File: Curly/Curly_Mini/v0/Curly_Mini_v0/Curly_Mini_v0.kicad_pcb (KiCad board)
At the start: 2 copper layers, 17 parts, among them U1 RP2040, U2 MCP25625T-E_ML, U4 W25Q16JVUXIQ_TR, Y2 12.000 MHz, C9002

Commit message: Curly Mini almost done :)
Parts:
- added C10: 100n, Capacitor_SMD:C_0402_1005Metric, F.Cu at (92.8, 58.1)
- added C11: 2u2, Capacitor_SMD:C_0402_1005Metric, F.Cu at (93.8, 57.1)
- added C12: 100n, Capacitor_SMD:C_0402_1005Metric, F.Cu at (78.1, 76.3)
- added C13: 2u2, Capacitor_SMD:C_0402_1005Metric, F.Cu at (79.8, 59.3)
- added C14: 100n, Capacitor_SMD:C_0402_1005Metric, F.Cu at (80.7, 59.3)
- added C15: 2u2, Capacitor_SMD:C_0402_1005Metric, F.Cu at (84.5, 52.2)
- added C16: 100n, Capacitor_SMD:C_0402_1005Metric, F.Cu at (84.5, 53.2)
- added C17: 100n, Capacitor_SMD:C_0402_1005Metric, F.Cu at (85.1, 64.5)
- added C18: 100n, Capacitor_SMD:C_0402_1005Metric, F.Cu at (89.3, 65.5)
- added C19: 2u2, Capacitor_SMD:C_0402_1005Metric, F.Cu at (84.2, 64.5)
- added C9: 2u2, Capacitor_SMD:C_0402_1005Metric, F.Cu at (82.2, 59.5)
- added J1: DEBUG_PORT, Connector_JST:JST_SH_BM03B-SRSS-TB_1x03-1MP_P1.00mm_Vertical, F.Cu at (75.8, 58.8)
- added J2: Conn_01x01_Pin, ICDB_Waffle:ICDB_Castellated_Pad, F.Cu at (121.0, 60.1)
- added J3: Conn_01x01_Pin, ICDB_Waffle:ICDB_Castellated_Pad, F.Cu at (121.0, 57.5)
- FB1: footprint Capacitor_SMD:C_0402_1005Metric -> Inductor_SMD:L_0603_1608Metric
- moved U4 25.9 mm to (80.7, 63.1), turned to 90 degrees
- moved FB1 25.4 mm to (84.2, 54.5), turned to 180 degrees
- moved C3 23.2 mm to (81.8, 55.8), turned to 180 degrees
- moved R4 22.2 mm to (80.2, 56.2), turned to -90 degrees
- moved C6 21.9 mm to (94.8, 56.7), turned to 90 degrees
- moved R3 21.7 mm to (79.2, 56.2), turned to -90 degrees
- moved C4 21.6 mm to (81.8, 54.5), turned to 180 degrees
- moved C5 21.2 mm to (83.3, 56.2), turned to 90 degrees
- moved C2 20.3 mm to (81.8, 56.8), turned to 180 degrees
- moved R1 19.4 mm to (81.6, 76.8)
- moved C7 18.7 mm to (97.6, 56.1), turned to 45 degrees
- moved Y2 17.0 mm to (98.5, 58.6), turned to 45 degrees
- moved C8 16.4 mm to (99.3, 61.0), turned to 45 degrees
- moved C1 15.8 mm to (79.5, 60.7), turned to 180 degrees
- moved U1 9.61 mm to (88.0, 59.4), turned to 90 degrees
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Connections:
- U1 pad 13: /SPI1_SCK -> unconnected-(U1-GPIO10-Pad13)
- U1 pad 14: /SPI1_TX -> unconnected-(U1-GPIO11-Pad14)
- U1 pad 17: unconnected-(U1-GPIO14-Pad17) -> /SPI1_SCK
- U1 pad 18: unconnected-(U1-GPIO15-Pad18) -> /SPI1_TX
- U2 pad 12: unconnected-(U2-CANL-Pad12) -> /CANL
- U2 pad 13: unconnected-(U2-CANH-Pad13) -> /CANH
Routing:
- net +1V1: track 0.00 -> 28.8 mm
- net +3V3: track 0.00 -> 22.5 mm, vias 0 -> 7
- net /SWCLK: track 0.00 -> 16.0 mm, vias 0 -> 2
- net /SWDIO: track 0.00 -> 15.3 mm, vias 0 -> 2
- net /SPI1_CSn: track 0.00 -> 14.9 mm
- net /SPI1_RX: track 0.00 -> 14.6 mm, vias 0 -> 2
- net /SPI1_TX: track 0.00 -> 14.5 mm, vias 0 -> 2
- net /SPI1_SCK: track 0.00 -> 14.4 mm
- net GND: track 0.00 -> 9.15 mm, vias 0 -> 41
- net /XIN: track 0.00 -> 8.95 mm
- net /~{QSPI_CSN}: track 0.00 -> 8.72 mm
- net /QSPI_SD1: track 0.00 -> 8.01 mm
- net /QSPI_SD2: track 0.00 -> 7.31 mm
- net Net-(U1-USB_DP): track 0.00 -> 6.11 mm
- net Net-(U1-USB_DM): track 0.00 -> 5.34 mm
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- added copper zone on F.Cu, net +3V3
- added copper zone on In1.Cu, net +3V3
- added copper zone on F.Cu, net GND
- added copper zone on In2.Cu, net GND
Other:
- copper layers 2 -> 4

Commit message: Curly Mini almost done (again) :)
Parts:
- removed C12: 100n, Capacitor_SMD:C_0402_1005Metric
- added C20: 10u, Capacitor_SMD:C_0603_1608Metric, F.Cu at (145.9, 56.9)
- added C21: 100n, Capacitor_SMD:C_0402_1005Metric, F.Cu at (142.4, 47.7)
- added C22: 10u, Capacitor_SMD:C_0603_1608Metric, F.Cu at (145.9, 59.4)
- added C23: 100n, Capacitor_SMD:C_0402_1005Metric, F.Cu at (142.4, 49.7)
- added C24: 100n, Capacitor_SMD:C_0402_1005Metric, F.Cu at (142.4, 51.6)
- added C25: 100n, Capacitor_SMD:C_0402_1005Metric, F.Cu at (105.7, 55.3)
- added C26: 100n, Capacitor_SMD:C_0402_1005Metric, F.Cu at (106.2, 63.8)
- added C27: 100n, Capacitor_SMD:C_0402_1005Metric, F.Cu at (142.4, 57.5)
- added C28: 2u2, Capacitor_SMD:C_0402_1005Metric, F.Cu at (142.4, 59.5)
- added C29: 2u2, Capacitor_SMD:C_0402_1005Metric, F.Cu at (105.7, 54.3)
- added U3: XC6206PxxxMR, Package_TO_SOT_SMD:SOT-23-3, F.Cu at (146.4, 48.9)
- added U5: SE8650X2-HF, Package_TO_SOT_SMD:SOT-23-3, F.Cu at (146.4, 53.4)
- moved R1 25.0 mm to (92.8, 54.5), turned to 180 degrees
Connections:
- U1 pad 11: unconnected-(U1-GPIO8-Pad11) -> /~{CAN_TX2_RTS}
- U1 pad 12: unconnected-(U1-GPIO9-Pad12) -> /~{CAN_TX1_RTS}
- U1 pad 13: unconnected-(U1-GPIO10-Pad13) -> /~{CAN_TX0_RTS}
- U1 pad 14: unconnected-(U1-GPIO11-Pad14) -> /~{CAN_RESET}
- U1 pad 27: unconnected-(U1-GPIO16-Pad27) -> /~{CAN_RX_INT}
- U1 pad 28: unconnected-(U1-GPIO17-Pad28) -> /~{CAN_RX_BUF0}
- U1 pad 29: unconnected-(U1-GPIO18-Pad29) -> /~{CAN_RX_BUF1}
- U1 pad 30: unconnected-(U1-GPIO19-Pad30) -> /MCP25625_CLK
- U1 pad 31: unconnected-(U1-GPIO20-Pad31) -> /CAN_TXVR_STBY
- U2 pad 10: unconnected-(U2-RXD-Pad10) -> Net-(U2-RXCAN)
- U2 pad 11: unconnected-(U2-VIO-Pad11) -> +3V3
- U2 pad 16: unconnected-(U2-TXD-Pad16) -> Net-(U2-TXCAN)
- U2 pad 18: unconnected-(U2-VSS-Pad18) -> GND
- U2 pad 19: unconnected-(U2-VDDA-Pad19) -> +5V
- U2 pad 2: unconnected-(U2-~{RESET}-Pad2) -> /~{CAN_RESET}
- U2 pad 21: unconnected-(U2-OSC1-Pad21) -> /MCP25625_CLK
- U2 pad 22: unconnected-(U2-GND-Pad22) -> GND
- U2 pad 23: unconnected-(U2-~{RX1BF}-Pad23) -> /~{CAN_RX_BUF1}
- U2 pad 24: unconnected-(U2-~{RX0BF}-Pad24) -> /~{CAN_RX_BUF0}
- U2 pad 25: unconnected-(U2-~{INT}-Pad25) -> /~{CAN_RX_INT}
- U2 pad 29: unconnected-(U2-EP-Pad29) -> GND
- U2 pad 3: unconnected-(U2-VDD-Pad3) -> +3V3
- U2 pad 4: unconnected-(U2-TXCAN-Pad4) -> Net-(U2-TXCAN)
- U2 pad 5: unconnected-(U2-RXCAN-Pad5) -> Net-(U2-RXCAN)
- U2 pad 7: unconnected-(U2-~{TX0RTS}-Pad7) -> /~{CAN_TX0_RTS}
- U2 pad 8: unconnected-(U2-~{TX1RTS}-Pad8) -> /~{CAN_TX1_RTS}
- U2 pad 9: unconnected-(U2-~{TX2RTS}-Pad9) -> /~{CAN_TX2_RTS}
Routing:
- net /~{CAN_TX2_RTS}: track 0.00 -> 26.6 mm
- net /CAN_TXVR_STBY: track 0.00 -> 23.9 mm
- net /~{CAN_TX1_RTS}: track 0.00 -> 23.7 mm
- net /~{CAN_TX0_RTS}: track 0.00 -> 21.6 mm
- net /MCP25625_CLK: track 0.00 -> 18.1 mm
- net /~{CAN_RESET}: track 0.00 -> 16.7 mm
- net /~{CAN_RX_BUF1}: track 0.00 -> 16.6 mm
- net /~{CAN_RX_INT}: track 0.00 -> 15.9 mm
- net /~{CAN_RX_BUF0}: track 0.00 -> 15.5 mm
- net Net-(U2-TXCAN): track 0.00 -> 11.7 mm, vias 0 -> 2
- net GND: track 9.15 -> 18.5 mm, vias 41 -> 56
- net Net-(U2-RXCAN): track 0.00 -> 7.33 mm, vias 0 -> 2
- net /~{EXT_RESET}: track 1.38 -> 4.56 mm, vias 1 -> 2
- net unconnected-(U1-GPIO16-Pad27): track 2.81 -> 0.00 mm
- net +5V: track 0.00 -> 2.33 mm
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
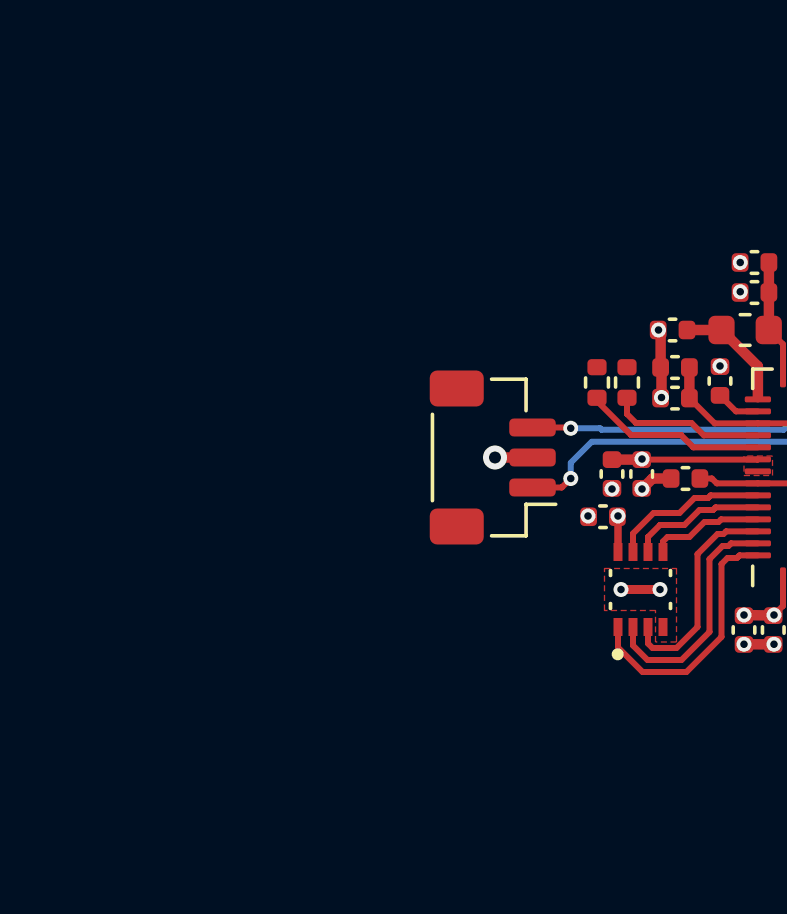
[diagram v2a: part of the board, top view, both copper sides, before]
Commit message: Curly Mini RS232 completed
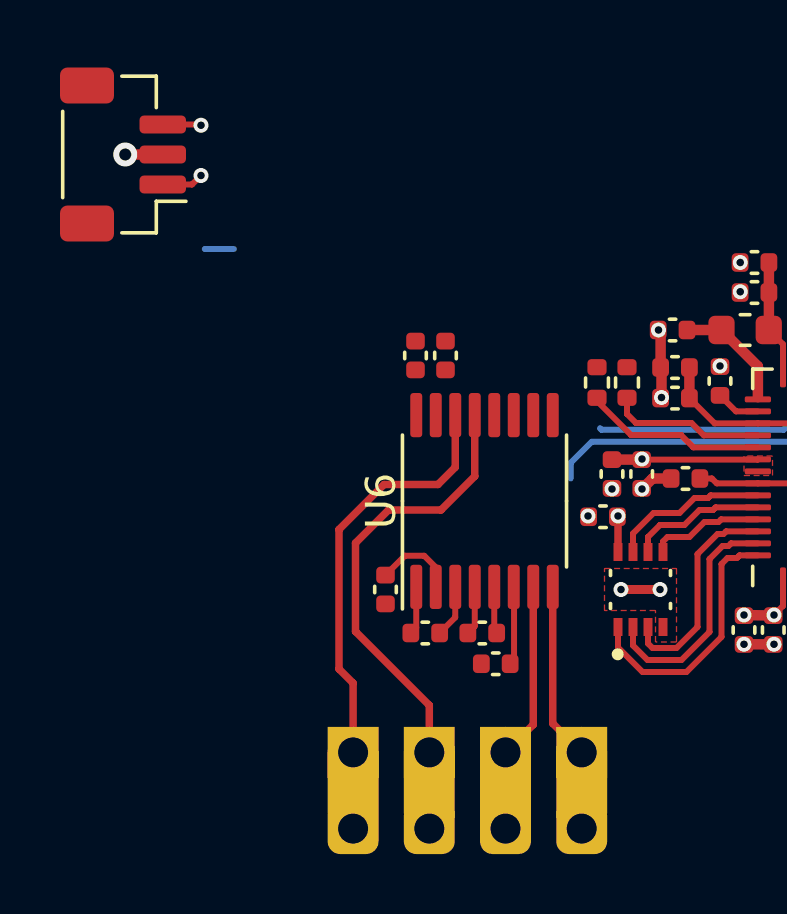
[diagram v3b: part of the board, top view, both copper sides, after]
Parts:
- added C12: 100n, Capacitor_SMD:C_0402_1005Metric, F.Cu at (75.4, 64.6)
- added C30: 100n, Capacitor_SMD:C_0402_1005Metric, F.Cu at (73.5, 64.6)
- added C31: 100n, Capacitor_SMD:C_0402_1005Metric, F.Cu at (75.9, 65.6)
- added C32: 100n, Capacitor_SMD:C_0402_1005Metric, F.Cu at (72.2, 63.1)
- added C33: 100n, Capacitor_SMD:C_0402_1005Metric, F.Cu at (73.2, 55.4)
- added C34: 2u2, Capacitor_SMD:C_0402_1005Metric, F.Cu at (74.2, 55.4)
- added J4: Conn_01x01_Pin, ICDB_Waffle:ICDB_Castellated_Pad, F.Cu at (76.2, 71.1)
- added J5: Conn_01x01_Pin, ICDB_Waffle:ICDB_Castellated_Pad, F.Cu at (78.7, 71.1)
- added J6: Conn_01x01_Pin, ICDB_Waffle:ICDB_Castellated_Pad, F.Cu at (71.1, 71.1)
- added J7: Conn_01x01_Pin, ICDB_Waffle:ICDB_Castellated_Pad, F.Cu at (73.7, 71.1)
- added U6: MAX3232, Package_SO:TSSOP-16_4.4x5mm_P0.65mm, F.Cu at (75.5, 60.2)
- moved J1 15.9 mm to (63.5, 48.6)
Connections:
- U1 pad 2: unconnected-(U1-GPIO0-Pad2) -> /UART_0_TX
- U1 pad 3: unconnected-(U1-GPIO1-Pad3) -> /UART_0_RX
- U1 pad 6: unconnected-(U1-GPIO4-Pad6) -> /UART_1_TX
- U1 pad 7: unconnected-(U1-GPIO5-Pad7) -> /UART_1_RX
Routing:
- net /RS232_0_RX: track 0.00 -> 14.9 mm
- net /RS232_0_TX: track 0.00 -> 14.1 mm
- net /RS232_1_RX: track 0.00 -> 5.92 mm
- net /RS232_1_TX: track 0.00 -> 5.90 mm
- net unconnected-(U1-GPIO0-Pad2): track 3.51 -> 0.00 mm
- net /UART_0_TX: track 0.00 -> 3.51 mm
- net Net-(U6-VS+): track 0.00 -> 2.75 mm
- net Net-(U6-VS-): track 0.00 -> 2.62 mm
- net Net-(U6-C1-): track 0.00 -> 1.75 mm
- net Net-(U6-C2+): track 0.00 -> 1.63 mm
- net Net-(U6-C1+): track 0.00 -> 1.61 mm
- net Net-(U6-C2-): track 0.00 -> 1.57 mm

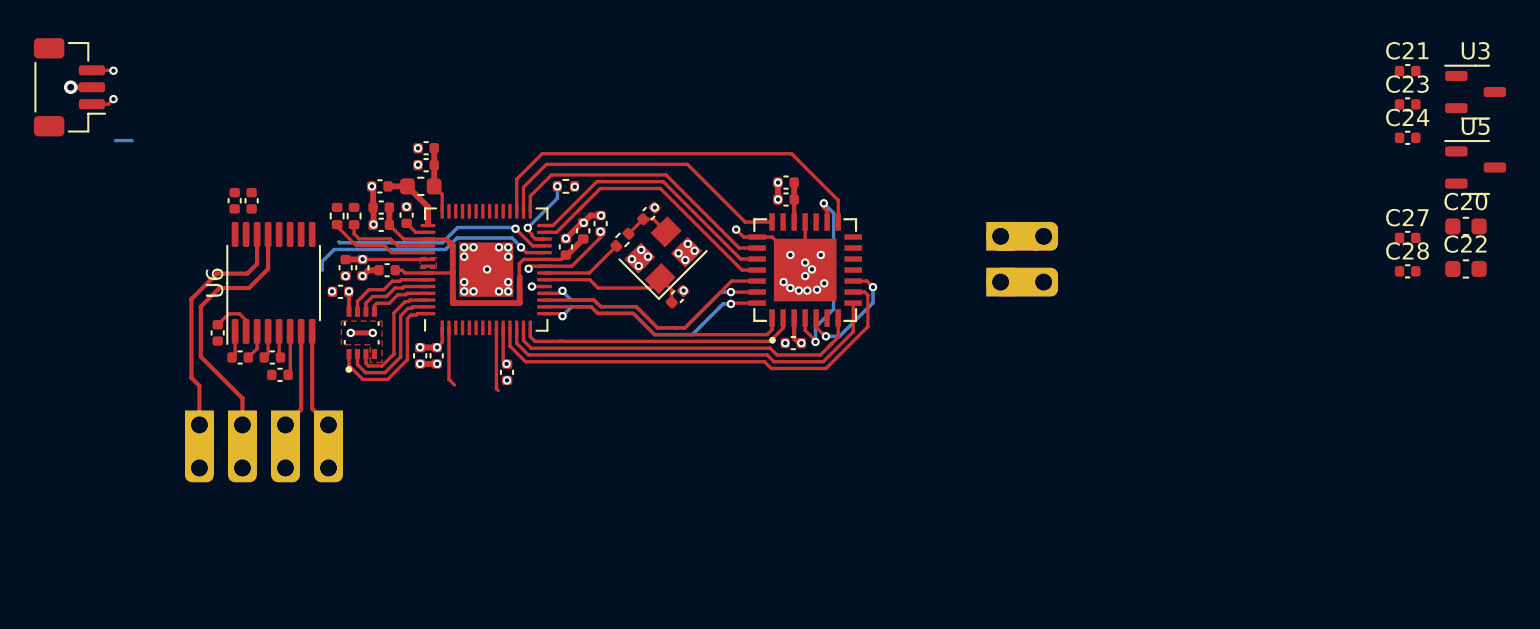
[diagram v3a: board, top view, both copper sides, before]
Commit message: Curly Mini Prelim layout done
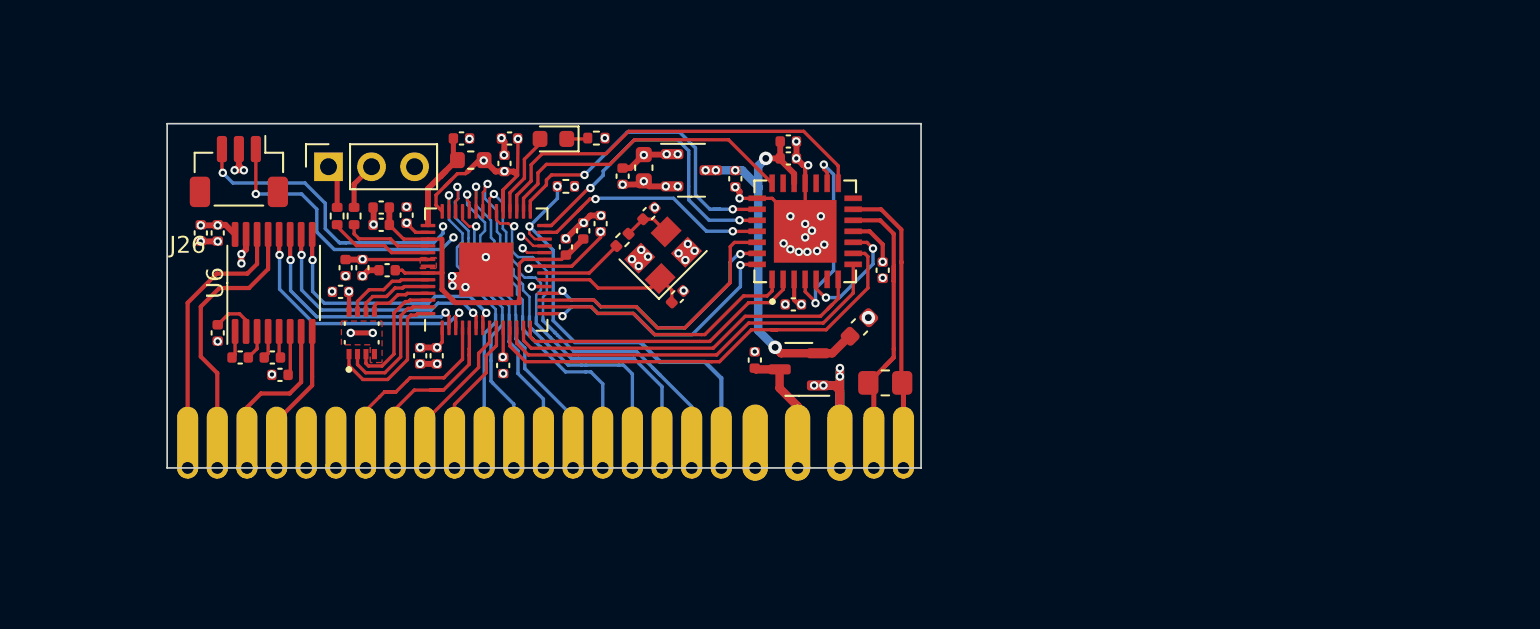
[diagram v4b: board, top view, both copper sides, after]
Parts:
- removed C28: 2u2, Capacitor_SMD:C_0402_1005Metric
- removed J2, J3, J4, J5, J6, J7: Conn_01x01_Pin, ICDB_Waffle:ICDB_Castellated_Pad
- added D1: LED, LED_SMD:LED_0603_1608Metric, F.Cu at (92.0, 51.7)
- added J26: Conn_01x24_Pin, ICDB_Curly:ICDB_Curly_Edge_Conn, F.Cu at (70.4, 71.1)
- added J8: SHORT_USB, Connector_PinSocket_2.54mm:PinSocket_1x03_P2.54mm_Vertical, F.Cu at (78.7, 53.3)
- added R5: 330R, Resistor_SMD:R_0402_1005Metric, F.Cu at (94.5, 51.6)
- added R6: 120R, Resistor_SMD:R_0805_2012Metric_Pad1.20x1.40mm_HandSolder, F.Cu at (111.6, 66.1)
- moved C20 48.6 mm to (97.3, 53.4), turned to 90 degrees
- moved C21 46.7 mm to (96.1, 53.9), turned to 90 degrees
- moved U3 46.5 mm to (100.2, 53.5)
- moved U5 41.7 mm to (106.5, 65.3), turned to 180 degrees
- moved C24 40.7 mm to (103.9, 64.8), turned to 90 degrees
- moved C23 39.9 mm to (102.8, 54.0), turned to -90 degrees
- moved C22 36.0 mm to (110.1, 62.8), turned to 45 degrees
- moved C27 31.0 mm to (111.5, 59.5), turned to -90 degrees
- moved J1 11.2 mm to (73.5, 53.6), turned to 180 degrees
- moved C4 5.59 mm to (86.6, 51.7), turned to 0 degrees
- moved C15 4.96 mm to (89.4, 51.7)
- moved C16 4.63 mm to (89.1, 53.1), turned to 90 degrees
- moved C34 3.55 mm to (71.2, 57.2), turned to -90 degrees
- moved C25 3.43 mm to (105.9, 51.9), turned to 0 degrees
- moved FB1 3.33 mm to (87.1, 53.0)
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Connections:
- U1 pad 32: unconnected-(U1-GPIO21-Pad32) -> Net-(D1-A)
- U1 pad 34: unconnected-(U1-GPIO22-Pad34) -> /GPIO_22
- U1 pad 35: unconnected-(U1-GPIO23-Pad35) -> /GPIO_23
- U1 pad 36: unconnected-(U1-GPIO24-Pad36) -> /GPIO_24
- U1 pad 37: unconnected-(U1-GPIO25-Pad37) -> /GPIO_25
- U1 pad 38: unconnected-(U1-GPIO26_ADC0-Pad38) -> /GPIO_26_A0
- U1 pad 39: unconnected-(U1-GPIO27_ADC1-Pad39) -> /GPIO_27_A1
- U1 pad 4: unconnected-(U1-GPIO2-Pad4) -> /GPIO_2
- U1 pad 40: unconnected-(U1-GPIO28_ADC2-Pad40) -> /GPIO_28_A2
- U1 pad 41: unconnected-(U1-GPIO29_ADC3-Pad41) -> /GPIO_29_A3
- U1 pad 5: unconnected-(U1-GPIO3-Pad5) -> /GPIO_3
- U1 pad 8: unconnected-(U1-GPIO6-Pad8) -> /GPIO_6
- U1 pad 9: unconnected-(U1-GPIO7-Pad9) -> /GPIO_7
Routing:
- net GND: track 18.5 -> 56.5 mm, vias 56 -> 68
- net /GPIO_25: track 0.00 -> 25.5 mm, vias 0 -> 1
- net /GPIO_23: track 0.00 -> 25.2 mm, vias 0 -> 1
- net /GPIO_24: track 0.00 -> 24.1 mm, vias 0 -> 1
- net /GPIO_22: track 0.00 -> 23.9 mm, vias 0 -> 1
- net /~{EXT_RESET}: track 4.56 -> 27.3 mm
- net +5V: track 2.33 -> 24.0 mm, vias 0 -> 5
- net /GPIO_28_A2: track 0.00 -> 21.2 mm, vias 0 -> 1
- net /GPIO_26_A0: track 0.00 -> 20.3 mm, vias 0 -> 1
- net +3V3: track 24.1 -> 43.1 mm, vias 9 -> 20
- net /CANL: track 0.00 -> 18.9 mm
- net /GPIO_29_A3: track 0.00 -> 18.7 mm, vias 0 -> 1
- net /GPIO_27_A1: track 0.00 -> 17.7 mm, vias 0 -> 1
- net /CANH: track 0.00 -> 17.5 mm
- net /UART_0_RX: track 0.00 -> 16.0 mm, vias 0 -> 2
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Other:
- board outline added: 44.5 x 20.3 mm
